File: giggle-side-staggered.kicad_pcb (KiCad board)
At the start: 2 copper layers, 97.5 x 97 mm, 42 parts, among them J1 CONN_05X2SHD, J2 CONN_05X2SHD

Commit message: yes.
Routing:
- net N-col-8: track 7.65 -> 0.00 mm
- net N-col-7: track 7.65 -> 0.00 mm
- net N-col-6: track 7.65 -> 0.00 mm
- net N-col-5: track 7.65 -> 0.00 mm
- net N-col-9: track 7.65 -> 0.00 mm
- net N-col-12: track 7.65 -> 0.00 mm
- net N-col-11: track 7.65 -> 0.00 mm
- net N-col-10: track 7.65 -> 0.00 mm
- net N-diode-19: track 0.00 -> 7.65 mm
- net N-diode-18: track 0.00 -> 7.65 mm
- net N-diode-17: track 0.00 -> 7.65 mm
- net N-diode-15: track 0.00 -> 7.65 mm
- net N-diode-14: track 0.00 -> 7.65 mm
- net N-diode-13: track 0.00 -> 7.65 mm
- net N-diode-11: track 0.00 -> 7.65 mm
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
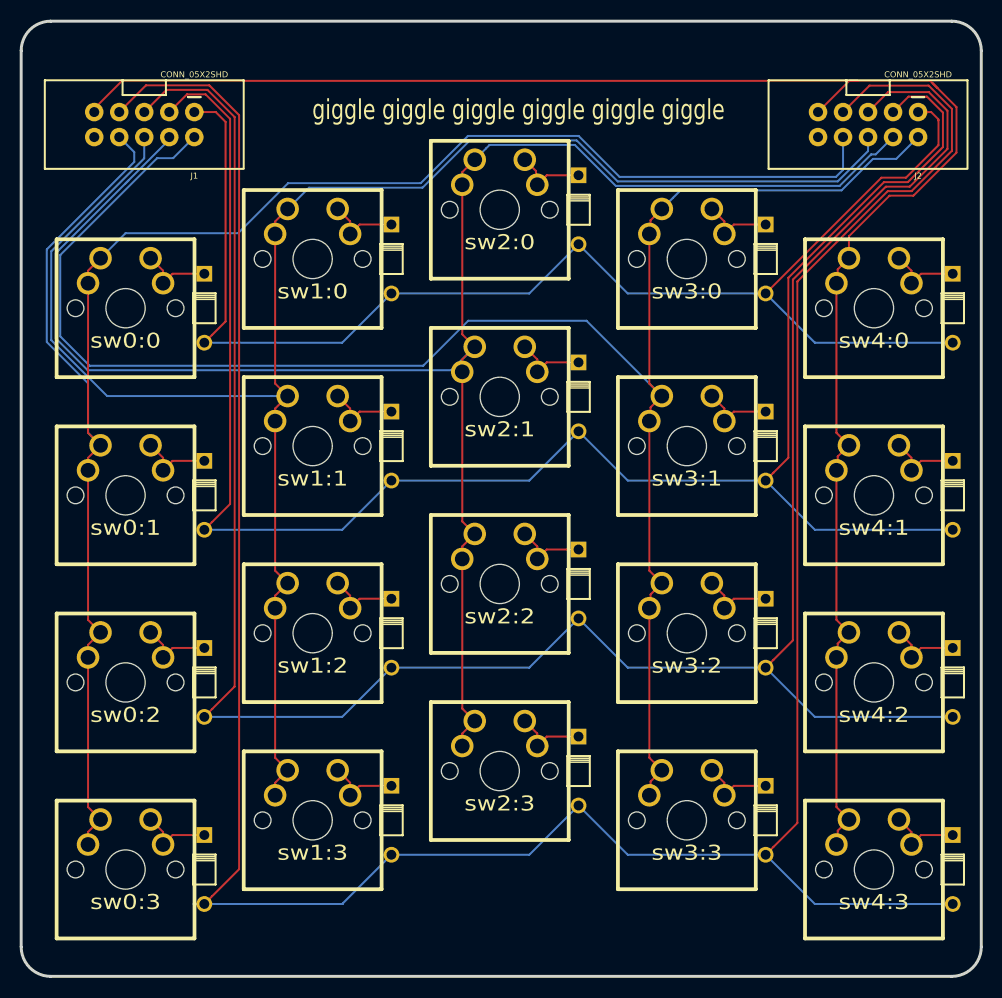
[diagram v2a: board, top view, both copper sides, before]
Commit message: changed switch's footprint and therefore changed the whole traces
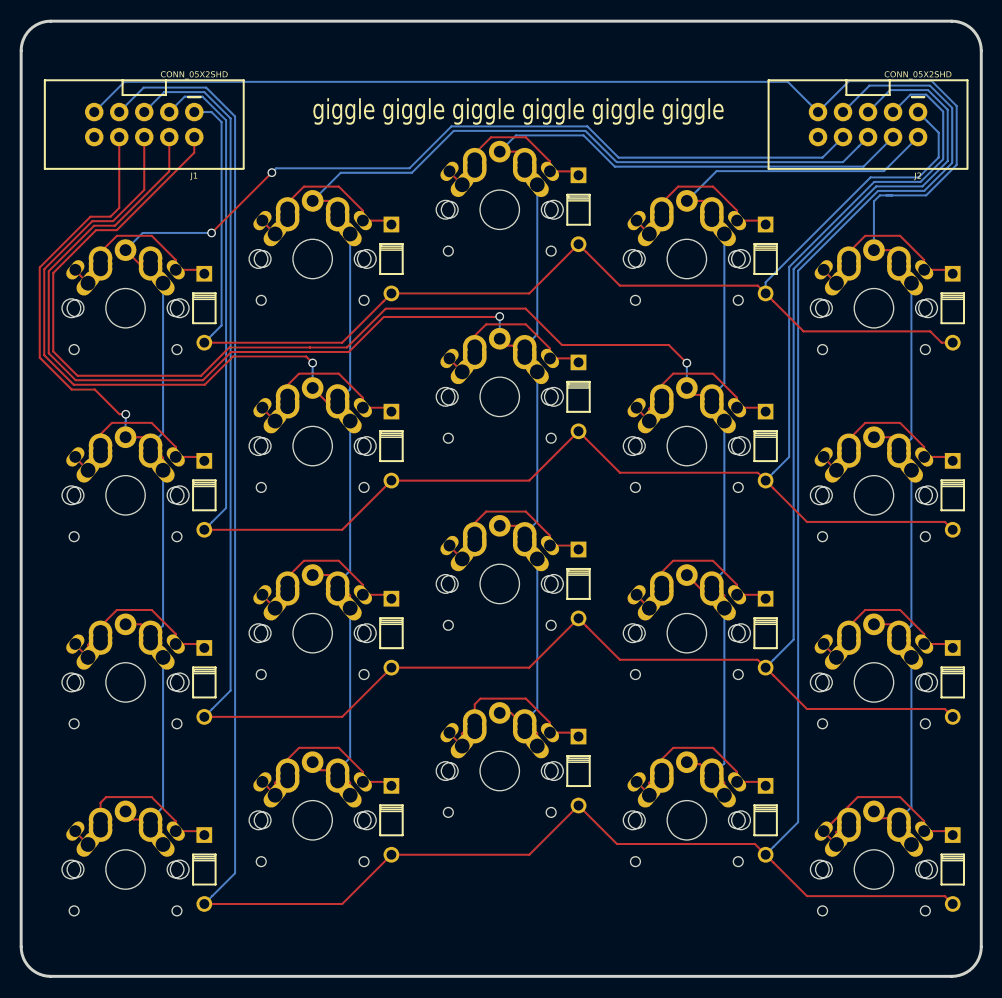
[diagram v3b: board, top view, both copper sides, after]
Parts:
- sw0:0, sw0:1, sw0:2, sw0:3, sw1:0, sw1:1, sw1:2, sw1:3, sw2:0, sw2:1, sw2:2, sw2:3, sw3:0, sw3:1, sw3:2, sw3:3, sw4:0, sw4:1, sw4:2, sw4:3: value (none) -> SW_PUSH; footprint MX_FLIP -> kbd:MX_ALPS_PG1350_noLed
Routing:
- net N-col-12: track 0.00 -> 19.9 mm
- net N-col-7: track 0.00 -> 19.6 mm
- net N-col-5: track 0.00 -> 19.5 mm
- net N-col-11: track 0.00 -> 19.5 mm
- net N-col-9: track 0.00 -> 19.5 mm
- net N-col-10: track 0.00 -> 19.3 mm
- net N-col-13: track 0.00 -> 19.0 mm
- net N-col-6: track 0.00 -> 18.8 mm
- net N-col-8: track 0.00 -> 18.5 mm
- net N-col-1: track 180.4 -> 195.7 mm, vias 0 -> 1
- net N-col-2: track 180.9 -> 196.1 mm, vias 0 -> 1
- net N-col-3: track 187.6 -> 202.5 mm, vias 0 -> 1
- net N-diode-10: track 7.65 -> 21.7 mm
- net N-diode-6: track 7.65 -> 20.5 mm
- net N-diode-4: track 7.65 -> 19.9 mm
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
